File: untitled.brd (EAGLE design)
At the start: 94 x 50 mm, 65 parts, among them IC1 SIM900, IC2 ST1S10PHR, IC3 SMF05C, IC5 BQ24072, IC6 SIM68R, X1 ST-SMB-H, X2 ST-SMB-H

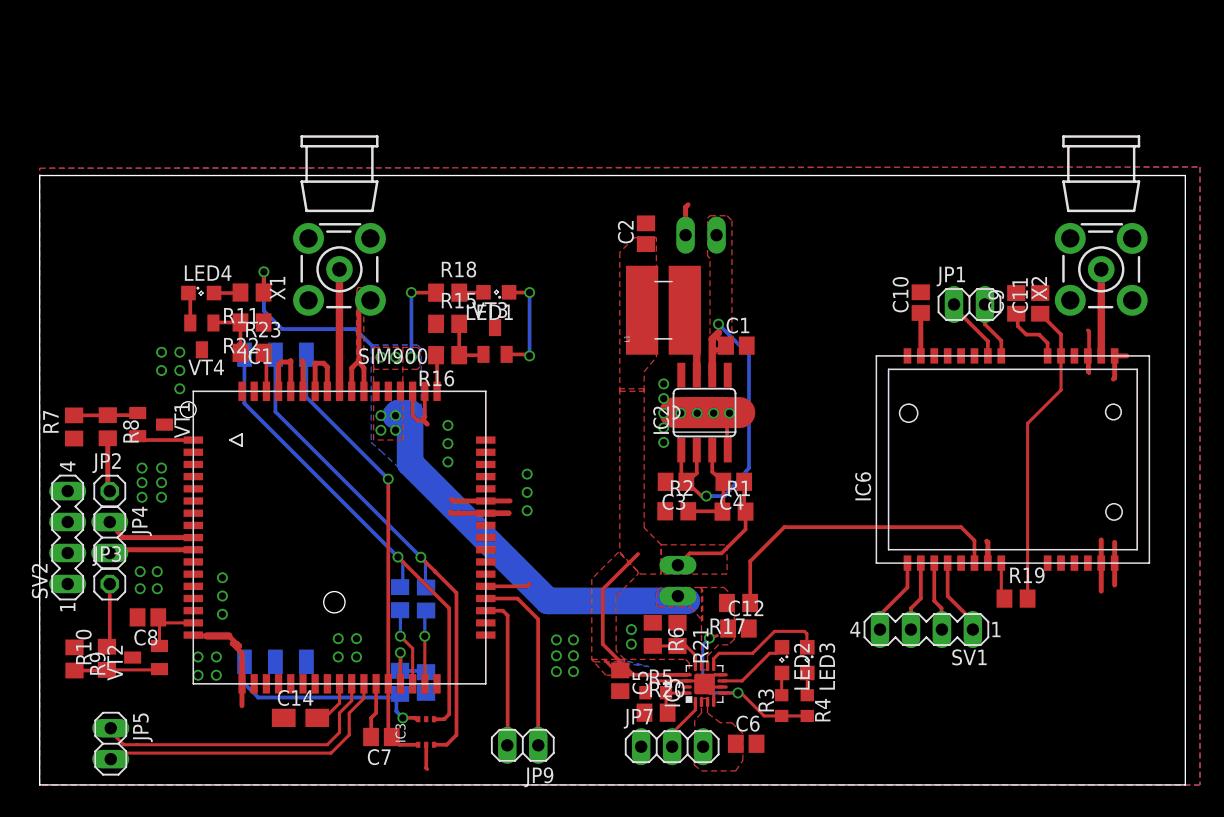
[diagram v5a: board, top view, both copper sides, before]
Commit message: Silkscreen issues solved
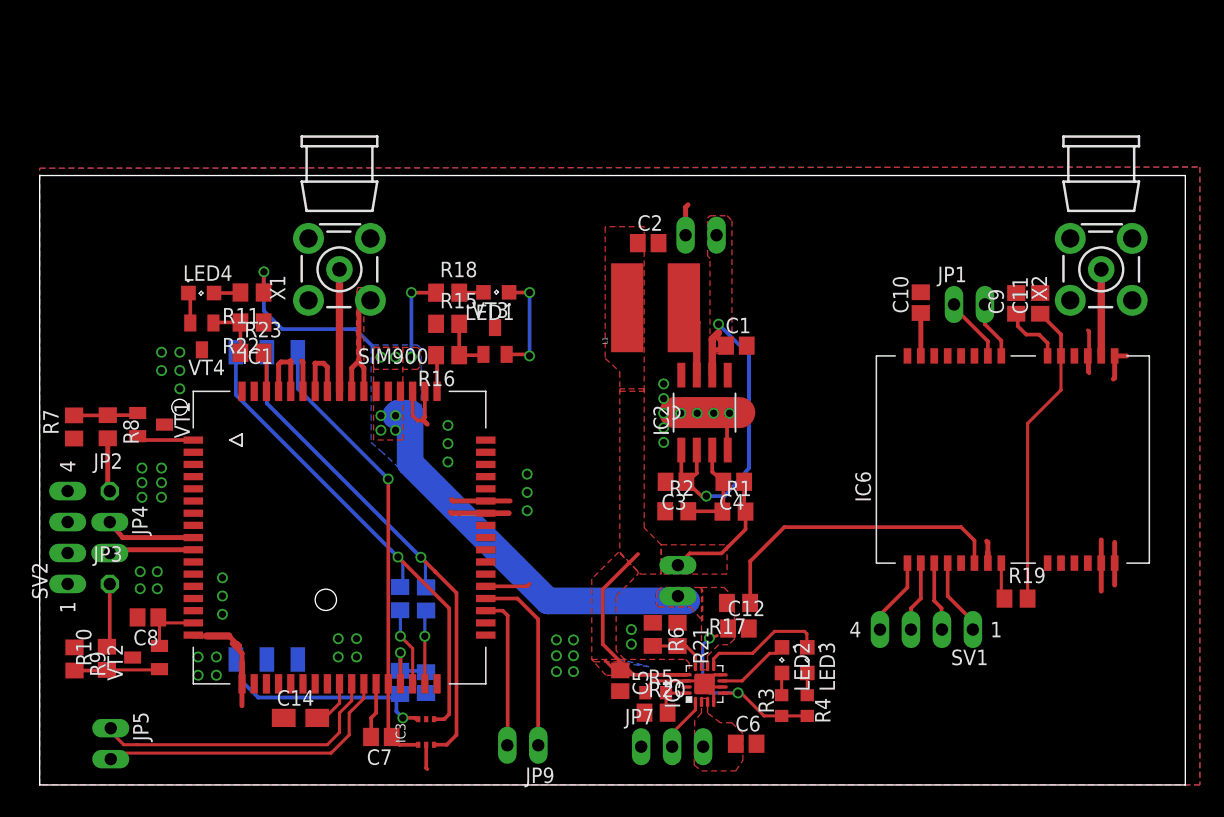
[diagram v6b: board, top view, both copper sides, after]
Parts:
- L1: device inductor-sumida-cdrh4d18:INDUCTOR-SUMIDA-CDRH4D18 -> CDRH6D38:INDUCTOR-SUMIDA-CDRH4D18
- moved C2 0.80 mm to (49.9, 44.5), turned to 0 degrees
- moved L1 0.73 mm to (50.5, 39.1)
- moved SIM2 0.73 mm to (16.1, 35.5)
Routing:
- net N$15: track 18.4 -> 19.0 mm
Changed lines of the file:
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@@
 <?xml version="1.0" encoding="utf-8"?>
 <!DOCTYPE eagle SYSTEM "eagle.dtd">
-<eagle version="6.4">
+<eagle version="6.5.0">
 <drawing>
 <settings>
@@
 <grid distance="0.1" unitdist="mm" unit="mm" style="lines" multiple="1" display="no" altdistance="0.025" altunitdist="inch" altunit="inch"/>
 <layers>
-<layer number="1" name="Top" color="4" fill="1" visible="yes" active="yes"/>
-<layer number="16" name="Bottom" color="1" fill="1" visible="no" active="yes"/>
+<layer number="1" name="Top" color="4" fill="1" visible="no" active="yes"/>
+<layer number="16" name="Bottom" color="1" fill="1" visible="yes" active="yes"/>
 <layer number="17" name="Pads" color="2" fill="1" visible="yes" active="yes"/>
 <layer number="18" name="Vias" color="2" fill="1" visible="yes" active="yes"/>
 <layer number="19" name="Unrouted" color="6" fill="1" visible="yes" active="yes"/>
 <layer number="20" name="Dimension" color="15" fill="1" visible="yes" active="yes"/>
-<layer number="21" name="tPlace" color="7" fill="1" visible="yes" active="yes"/>
-<layer number="22" name="bPlace" color="7" fill="1" visible="no" active="yes"/>
-<layer number="23" name="tOrigins" color="15" fill="1" visible="yes" active="yes"/>
-<layer number="24" name="bOrigins" color="15" fill="1" visible="no" active="yes"/>
+<layer number="21" name="tPlace" color="7" fill="1" visible="no" active="yes"/>
+<layer number="22" name="bPlace" color="7" fill="1" visible="yes" active="yes"/>
+<layer number="23" name="tOrigins" color="15" fill="1" visible="no" active="yes"/>
+<layer number="24" name="bOrigins" color="15" fill="1" visible="yes" active="yes"/>
 <layer number="25" name="tNames" color="7" fill="1" visible="no" active="yes"/>
 <layer number="26" name="bNames" color="7" fill="1" visible="no" active="yes"/>
 <layer number="27" name="tValues" color="7" fill="1" visible="no" active="yes"/>
 <layer number="28" name="bValues" color="7" fill="1" visible="no" active="yes"/>
-<layer number="29" name="tStop" color="7" fill="3" visible="yes" active="yes"/>
-<layer number="30" name="bStop" color="7" fill="6" visible="no" active="yes"/>
+<layer number="29" name="tStop" color="7" fill="3" visible="no" active="yes"/>
+<layer number="30" name="bStop" color="7" fill="6" visible="yes" active="yes"/>
 <layer number="31" name="tCream" color="7" fill="4" visible="no" active="yes"/>
 <layer number="32" name="bCream" color="7" fill="5" visible="no" active="yes"/>
 <layer number="33" name="tFinish" color="6" fill="3" visible="no" active="yes"/>
-<layer number="34" name="bFinish" color="6" fill="6" visible="yes" active="yes"/>
+<layer number="34" name="bFinish" color="6" fill="6" visible="no" active="yes"/>
 <layer number="35" name="tGlue" color="7" fill="4" visible="no" active="yes"/>
-<layer number="36" name="bGlue" color="7" fill="5" visible="yes" active="yes"/>
+<layer number="36" name="bGlue" color="7" fill="5" visible="no" active="yes"/>
 <layer number="37" name="tTest" color="7" fill="1" visible="no" active="yes"/>
-<layer number="38" name="bTest" color="7" fill="1" visible="yes" active="yes"/>
+<layer number="38" name="bTest" color="7" fill="1" visible="no" active="yes"/>
 <layer number="39" name="tKeepout" color="4" fill="11" visible="no" active="yes"/>
 <layer number="40" name="bKeepout" color="1" fill="11" visible="no" active="yes"/>
@@
 <layer number="50" name="dxf" color="7" fill="1" visible="no" active="no"/>
 <layer number="51" name="tDocu" color="7" fill="1" visible="no" active="yes"/>
-<layer number="52" name="bDocu" color="7" fill="1" visible="no" active="yes"/>
+<layer number="52" name="bDocu" color="7" fill="1" visible="yes" active="yes"/>
 <layer number="53" name="tGND_GNDA" color="7" fill="9" visible="no" active="no"/>
 <layer number="54" name="bGND_GNDA" color="1" fill="9" visible="no" active="no"/>
@@
 </class>
 </classes>
-<designrules name="SeeedStudio_DRU_no_angle_20130527 *">
+<designrules name="SeeedStudio_DRU_no_angle_20130527">
 <description language="de">&lt;b&gt;EAGLE Design Rules&lt;/b&gt;
 &lt;p&gt;
@@
 </description>
 <param name="layerSetup" value="(1*2*15*16)"/>
-<param name="mtCopper" value="0.035mm 0mil 0.035mm 0.035mm 0.035mm 0.035mm 0.035mm 0.035mm 0.035mm 0.035mm 0.035mm 0.035mm 0.035mm 0.035mm 0mil 0.035mm"/>
+<param name="mtCopper" value="0.035mm 0.0175mm 0.035mm 0.035mm 0.035mm 0.035mm 0.035mm 0.035mm 0.035mm 0.035mm 0.035mm 0.035mm 0.035mm 0.035mm 0.0175mm 0.035mm"/>
 <param name="mtIsolate" value="0.2mm 1.1mm 0.2mm 0.15mm 0.2mm 0.15mm 0.2mm 0.15mm 0.2mm 0.15mm 0.2mm 0.15mm 0.2mm 0.15mm 0.2mm"/>
 <param name="mdWireWire" value="6mil"/>
@@
 <element name="IC2" library="vreg-pulse (1)" package="HSOP8" value="ST1S10PHR" x="54.55" y="30.55"/>
 <element name="C1" library="resistor" package="C0805" value="10u" x="57.165" y="36.0425"/>
-<element name="C2" library="resistor" package="C0805" value="22u" x="49.7475" y="45.2275" rot="R90"/>
+<element name="C2" library="resistor" package="C0805" value="22u" x="49.9275" y="44.4525"/>
 <element name="C3" library="resistor" package="C0805" value="4.7u" x="52.21" y="24.87" rot="R180"/>
 <element name="C4" library="resistor" package="C0805" value="4.7n" x="56.9475" y="24.8725" rot="R180"/>
-<element name="L1" library="inductor-sumida-cdrh4d18" package="INDUCTOR-SUMIDA-CDRH4D18" value="INDUCTOR-SUMIDA-CDRH4D18" x="51.2325" y="38.95" rot="R90"/>
+<element name="L1" library="CDRH6D38" package="INDUCTOR-SUMIDA-CDRH4D18" value="INDUCTOR-SUMIDA-CDRH4D18" x="50.5325" y="39.15" rot="R90"/>
 <element name="R1" library="rcl" package="R0805" value="100k" x="56.9675" y="22.4275"/>
 <element name="R2" library="rcl" package="R0805" value="20k" x="52.27" y="22.4525"/>
@@
 <attribute name="OC_FARNELL" value="unknown" x="24.6" y="42.3" size="1.778" layer="27" rot="R90" display="off"/>
 </element>
-<element name="SIM2" library="ICA-501" package="ICA-501-006-F7" value="ICA-501" x="16.8" y="35.3" rot="MR270"/>
+<element name="SIM2" library="ICA-501" package="ICA-501-006-F7" value="ICA-501" x="16.1" y="35.5" rot="MR270"/>
 <element name="C13" library="resistor" package="C0805" value="18p" x="31.7" y="8.4" rot="MR270"/>
 <element name="C14" library="rcl" package="A/3216-18R" value="" x="21.4" y="5.5"/>
@@
 <contactref element="L1" pad="P$1"/>
 <wire x1="53.915" y1="33.6234" x2="53.915" y2="37.9675" width="0.6096" layer="1"/>
-<wire x1="53.915" y1="37.9675" x2="52.9325" y2="38.95" width="0.6096" layer="1"/>
+<wire x1="53.915" y1="37.9675" x2="52.8575" y2="39.15" width="0.6096" layer="1"/>
 </signal>
 <signal name="+4.8V">
@@
 <contactref element="C5" pad="1"/>
 <polygon width="0.3048" layer="1" thermals="no">
-<vertex x="50.6" y="44.9"/>
-<vertex x="48.8" y="44.9"/>
-<vertex x="47.6" y="43.7"/>
+<vertex x="46.4" y="45.8"/>
+<vertex x="46.4" y="35"/>
+<vertex x="47.6" y="33.9"/>
 <vertex x="47.6" y="32.3"/>
 <vertex x="49.6" y="32.3"/>
-<vertex x="49.6" y="33.9"/>
-<vertex x="50.6" y="35.1"/>
+<vertex x="49.6" y="45.8"/>
 </polygon>
 <polygon width="0.3048" layer="1" thermals="no">
@@
 <contactref element="C7" pad="1"/>
 <contactref element="SIM2" pad="VCC"/>
-<wire x1="28.6" y1="25.1" x2="21.88" y2="31.82" width="0.3048" layer="16"/>
-<wire x1="21.88" y1="35.3" x2="21.88" y2="31.82" width="0.3048" layer="16"/>
 <wire x1="28.605" y1="8.295" x2="28.605" y2="4.22" width="0.3048" layer="1"/>
 <wire x1="28.605" y1="4.22" x2="28.89" y2="3.935" width="0.3048" layer="1"/>
@@
 <wire x1="28.605" y1="8.295" x2="28.605" y2="25.095" width="0.3048" layer="1"/>
 <wire x1="28.605" y1="25.095" x2="28.6" y2="25.1" width="0.3048" layer="1"/>
+<wire x1="21.18" y1="35.5" x2="21.18" y2="32.52" width="0.3048" layer="16"/>
+<wire x1="21.18" y1="32.52" x2="28.6" y2="25.1" width="0.3048" layer="16"/>
 </signal>
 <signal name="SIM_DATA">
@@
 <contactref element="IC3" pad="3"/>
 <contactref element="SIM2" pad="RESET"/>
-<wire x1="19.34" y1="35.3" x2="19.34" y2="30.615" width="0.3048" layer="16"/>
 <wire x1="34.2" y1="4.1" x2="33.4" y2="3.3" width="0.3048" layer="1"/>
 <wire x1="33.4" y1="3.3" x2="32.37" y2="3.3" width="0.3048" layer="1"/>
@@
 <wire x1="34.2" y1="4.1" x2="34.2" y2="15.755" width="0.3048" layer="1"/>
 <wire x1="34.2" y1="15.755" x2="32.455" y2="17.5" width="0.3048" layer="1"/>
-<wire x1="19.34" y1="30.615" x2="31.2775" y2="18.6775" width="0.3048" layer="16"/>
 <wire x1="31.2775" y1="18.6775" x2="31.655" y2="18.3" width="0.3048" layer="16"/>
 <wire x1="32.455" y1="17.5" x2="32.45" y2="17.5" width="0.3048" layer="1"/>
@@
 <wire x1="31.2775" y1="18.6775" x2="31.2775" y2="18.6725" width="0.3048" layer="16"/>
 <wire x1="31.2775" y1="18.6725" x2="31.65" y2="18.3" width="0.3048" layer="16"/>
+<wire x1="18.64" y1="35.5" x2="18.64" y2="31.315" width="0.3048" layer="16"/>
+<wire x1="18.64" y1="31.315" x2="31.2775" y2="18.6775" width="0.3048" layer="16"/>
 </signal>
 <signal name="N$18">
@@
 <contactref element="IC3" pad="4"/>
 <contactref element="SIM2" pad="CLOCK"/>
-<wire x1="29.4" y1="18.7" x2="16.8" y2="31.3" width="0.3048" layer="16"/>
-<wire x1="16.8" y1="31.3" x2="16.8" y2="35.3" width="0.3048" layer="16"/>
 <wire x1="32.365" y1="5.395" x2="33.195" y2="5.395" width="0.3048" layer="1"/>
 <wire x1="33.195" y1="5.395" x2="33.6" y2="5.8" width="0.3048" layer="1"/>
@@
 <via x="29.4" y="18.7" extent="1-16" drill="0.6"/>
 <wire x1="29.4" y1="18.7" x2="29.8" y2="18.3" width="0.3048" layer="16"/>
+<wire x1="16.1" y1="35.5" x2="16.1" y2="32" width="0.3048" layer="16"/>
+<wire x1="16.1" y1="32" x2="29.4" y2="18.7" width="0.3048" layer="16"/>
 </signal>
 <signal name="SIM_PRESENCE">
@@
 <wire x1="17.93" y1="7.17" x2="16.7" y2="8.4" width="0.3048" layer="16"/>
 <wire x1="16.7" y1="8.4" x2="16.7" y2="10" width="0.3048" layer="16"/>
-<wire x1="16.7" y1="10" x2="16.8" y2="10.1" width="0.3048" layer="16"/>
+<wire x1="16.7" y1="10" x2="16.1" y2="10.3" width="0.3048" layer="16"/>
 <wire x1="29.27" y1="7.17" x2="29.565" y2="7.465" width="0.3048" layer="16"/>
 <wire x1="29.27" y1="7.17" x2="29.27" y2="6.03" width="0.3048" layer="16"/>

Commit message: small changes
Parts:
- removed IC6: SIM68R, sim68:SIM68
- added IC4: SIM900, sim900R:SIM900
- C10: value 1u -> 22u
- C11: value 1u -> 100n
- C12: value 4.7u -> (none); device resistor:C0805 -> rcl:A/3216-18R
- C13: value 18p -> 100n
- C14: value (none) -> 18p; device rcl:A/3216-18R -> resistor:C0805
- C2: value 22u -> 4.7u
- C3: value 4.7u -> 1u
- C4: value 4.7n -> 4.7u
- C7, C8: value 100n -> 1u
- C9: value 1u -> 4.7n
- IC1: value SIM900 -> SIM68R; device sim900R:SIM900 -> sim68:SIM68
- IC3: value SMF05C -> BQ24072; device smf05c:SC-70-6 -> TI-bq24075:QFN16
- IC5: value BQ24072 -> SMF05C; device TI-bq24075:QFN16 -> smf05c:SC-70-6
- JP2: device pinhead:1X01 -> pinhead:1X03
- JP3: device pinhead:1X01 -> pinhead:1X02
- JP5, JP6: device pinhead:1X02 -> pinhead:1X01
- JP7: device pinhead:1X03 -> pinhead:1X02
- R1: value 100k -> 33
- R10, R8: value 4.7k -> 20k
- R11: value 150 -> 4.7k
- R12: value 22 -> 4.7k
- R13, R14: value 22 -> 47k
- R15: value 47k -> 4.7k
- R16: value 4.7k -> 47k
- R17: value 33 -> 150
- R18: value 150 -> 22
- R19: value 10 -> 22
- R2: value 20k -> 10
- R20: value 20k -> 4.7k
- R21: value 3.3k -> 47k
- R22: value 47k -> 150
- R23: value 4.7k -> 22
- R3: value 1.5k -> 1.8k; device rcl:R0603 -> rcl:R0805
- R4: value 1.5k -> 3.3k; device rcl:R0603 -> rcl:R0805
- R5: value 1.2k -> 1.5k
- R6: value 1.8k -> 1.5k; device rcl:R0805 -> rcl:R0603
- R7: value 47k -> 1.2k; device rcl:R0805 -> rcl:R0603
- R9: value 47k -> 100k
- moved C11 77.8 mm to (8.69, 13.7), turned to 180 degrees
- moved C8 75.7 mm to (80.0, 39.5), turned to 90 degrees
- moved JP4 73.1 mm to (76.3, 39.4), turned to 0 degrees
- moved C7 64.7 mm to (82.1, 39.5), turned to 90 degrees
- moved JP8 63.9 mm to (5.83, 3.38), flipped to the top, turned to 270 degrees
- moved X1 62.5 mm to (87.1, 42.3)
- moved X2 62.5 mm to (24.6, 42.3)
- moved LED3 58.1 mm to (13.3, 40.4), turned to 0 degrees
- moved R9 55.4 mm to (57.0, 22.4), turned to 0 degrees
- moved R7 52.4 mm to (50.5, 7.67), turned to 0 degrees
- moved JP2 51.1 mm to (52.2, 2.84)
- moved R8 50.9 mm to (50.6, 5.53), turned to 0 degrees
- moved R19 50.5 mm to (29.6, 15.3), flipped to the bottom, turned to 270 degrees
- moved JP7 49.2 mm to (5.75, 20.3), turned to 270 degrees
- moved R10 48.3 mm to (52.3, 22.5), turned to 0 degrees
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- renumbered SIM2 to SIM1
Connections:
- removed net N$16 (its old number): LED1.C, VT3.C
- new net N$37: LED3.C, VT3.C
- net +12V: now also C2.1, JP1.2; no longer C3.1, JP8.2
- net +4.8V: now also C10.1, C3.1, C9.1, IC3.13, JP3.1, R9.2; no longer C2.1, C4.1, C5.1, IC5.13, JP6.1, R1.2
- net BAT: now also C4.1, IC3.2, IC3.3, JP2.3; no longer C6.1, IC5.2, IC5.3, JP7.3
- net DBG_RXD: now also IC4.28, JP8.2; no longer IC1.28, JP5.2
- net DBG_TXD: now also IC4.27, JP8.1; no longer IC1.27, JP5.1
- net GND: now also C12.-, C14.2, C4.2, IC1.13, IC1.14, IC1.15, IC1.7, IC3.14, IC3.4, IC3.6, IC3.8, IC3.TH, IC4.17, IC4.18, IC4.29, IC4.39, IC4.45, IC4.46, IC4.53, IC4.54, IC4.58, IC4.59, IC4.61, IC4.62, IC4.63, IC4.64, IC4.65, IC5.2, JP1.1, JP2.1, R10.1, R13.1, R14.1, R16.1, R3.1, R4.1, R8.1; no longer C12.2, C14.-, C9.2, IC1.18, IC1.29, IC1.39, IC1.45, IC1.46, IC1.53, IC1.54, IC1.58, IC1.59, IC1.61, IC1.62, IC1.63, IC1.64, IC1.65, IC3.2, IC5.14, IC5.4, IC5.6, IC5.8, IC5.TH, IC6.13, IC6.14, IC6.15, IC6.17, IC6.7, JP7.1, JP8.1, R15.1, R2.1, R20.1, R22.1, R5.1, R6.1, R9.1
- net N$10: now also IC4.1; no longer IC1.1
- net N$11: now also R11.1, R13.2; no longer R7.2, R8.1
- net N$12: now also R12.1, R14.2; no longer R10.1, R9.2
- net N$13: now also IC4.60, X2.1; no longer IC1.60, X1.1
- net N$14: now also IC5.3, R18.1; no longer IC3.3, R12.1
- net N$15: now also IC5.6, R23.2; no longer IC3.6, R14.2
- net N$17: now also C12.+, IC4.26; no longer C14.+, IC1.26
- net N$18: now also IC5.4, R19.1; no longer IC3.4, R13.1
- net N$19: now also R20.1, R21.2, VT4.B; no longer R15.2, R16.1, VT3.B
- net N$2: now also C11.1, IC4.16; no longer C8.1, IC1.16
- net N$20: now also IC4.52, R20.2; no longer IC1.52, R16.2
- net N$21: now also IC1.6, R1.1; no longer IC6.6, R17.1
- net N$22: now also IC1.8, R2.1; no longer IC6.8, R19.1
- net N$23: now also C7.1, IC1.19, R2.2; no longer C11.1, IC6.19, R19.2
- net N$24: now also IC1.16, X1.1; no longer IC6.16, X2.1
- net N$25: now also IC1.22, JP4.1; no longer IC6.22, JP1.1
- net N$26: now also C8.1, IC1.20; no longer C9.1, IC6.20
- net N$27: now also C5.1, IC1.27; no longer C10.1, IC6.27
- net N$28: now also IC1.4; no longer IC6.4
- net N$29: now also IC1.3; no longer IC6.3
- net N$3: now also C9.2, R10.2, R9.1; no longer C4.2, R1.1, R2.2
- net N$30: now also IC1.2; no longer IC6.2
- net N$31: now also IC1.1; no longer IC6.1
- net N$32: now also IC1.21, JP4.2; no longer IC6.21, JP1.2
- net N$33: now also IC4.38; no longer IC1.38
- net N$34: now also IC4.37; no longer IC1.37
- net N$35: now also R15.1, R16.2, VT3.B; no longer R22.2, R23.1, VT4.B
- net N$36: now also LED3.A, R17.2; no longer LED4.A, R11.2
- net N$38: now also IC4.66, R15.2; no longer IC1.66, R23.2
- net N$4: now also LED2.A, R6.1; no longer LED3.A, R4.1
- net N$45: now also LED4.A, R22.2; no longer LED1.A, R18.2
- net N$5: now also IC3.16, R7.2, R8.2; no longer IC5.16, R20.2, R5.2
- net N$6: now also IC3.12, R3.2, R4.2; no longer IC5.12, R21.2, R6.2
- net N$7: now also LED1.A, R5.2; no longer LED2.A, R3.2
- net N$8: now also IC3.9, LED2.C; no longer IC5.9, LED3.C
- net N$9: now also IC3.7, LED1.C; no longer IC5.7, LED2.C
- net POWER: now also JP5.1, R11.2; no longer JP2.1, R8.2
- net RESET: now also JP6.1, R12.2; no longer JP3.1, R10.2
- net RXD: now also IC4.10, JP7.2; no longer IC1.10, JP4.2
- net SIM_CLK: now also IC4.32, R19.2; no longer IC1.32, R13.2
- net SIM_DATA: now also C14.1, IC4.31, R23.1; no longer C13.1, IC1.31, R14.1
- net SIM_PRESENCE: now also IC4.34; no longer IC1.34
- net SIM_RST: now also IC4.33, R18.2; no longer IC1.33, R12.2
- net SIM_VDD: now also C13.1, IC4.30, IC5.1; no longer C7.1, IC1.30, IC3.1
- net TS: now also IC3.1, JP2.2; no longer IC5.1, JP7.2
- net TXD: now also IC4.9, JP7.1; no longer IC1.9, JP4.1
- net VBAT: now also C6.1, IC3.10, IC3.11, IC3.5, IC4.55, IC4.56, IC4.57, JP3.2, R1.2, R17.1, R22.1, R5.1, R6.2; no longer C12.1, IC1.55, IC1.56, IC1.57, IC5.10, IC5.11, IC5.5, JP6.2, R11.1, R17.2, R18.1, R3.1, R4.2
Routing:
- net N$16 (its old number): track 8.83 -> 0.00 mm, vias 2 -> 0
- net N$16: track 2.52 -> 8.83 mm, vias 0 -> 2
- net N$37: track 0.00 -> 2.52 mm
- net N$5: track 3.39 -> 3.94 mm
- net GND: track 105.6 -> 105.5 mm, vias 49 -> 62
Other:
- board text added: "Designed by cap"
